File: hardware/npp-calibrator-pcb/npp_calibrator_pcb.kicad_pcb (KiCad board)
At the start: 2 copper layers, 80 x 34 mm, 7 parts, among them X1 SOIC16 Test Socket, X2 DE9_Plug, X3 DE9_Plug

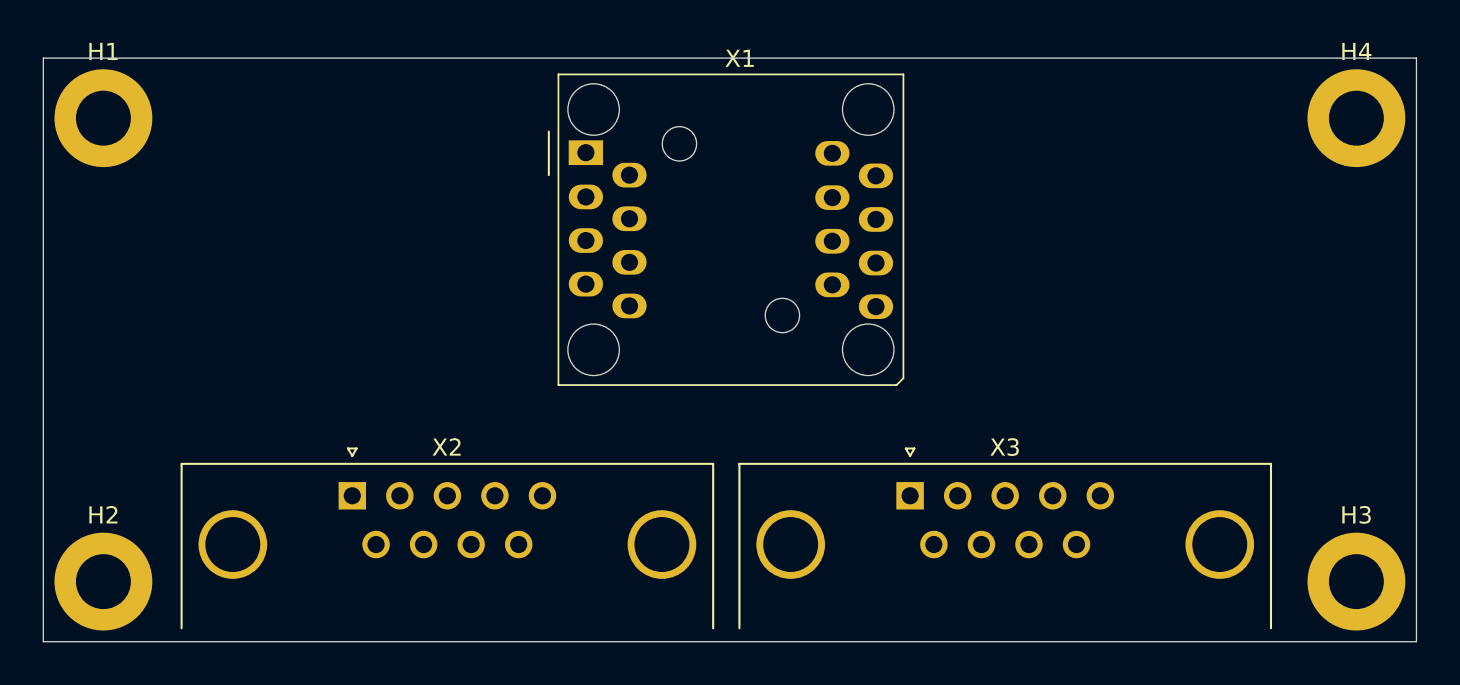
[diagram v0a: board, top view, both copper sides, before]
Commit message: Updates to calibration hardware
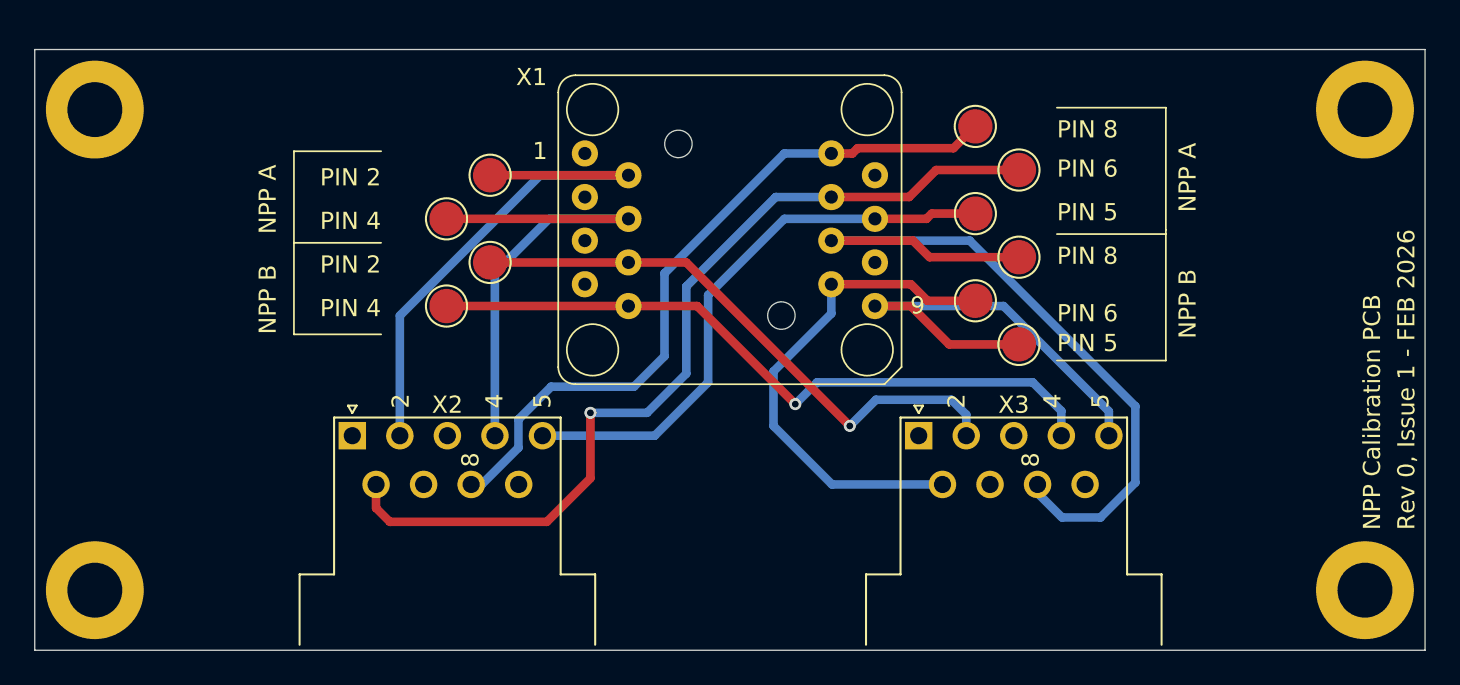
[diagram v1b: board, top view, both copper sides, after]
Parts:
- added TP1: TestPoint, TestPoint:TestPoint_Pad_D2.0mm, F.Cu at (114.3, 99.1)
- added TP10: TestPoint, TestPoint:TestPoint_Pad_D2.0mm, F.Cu at (114.3, 104.1)
- added TP2: TestPoint, TestPoint:TestPoint_Pad_D2.0mm, F.Cu at (83.5, 99.4)
- added TP3: TestPoint, TestPoint:TestPoint_Pad_D2.0mm, F.Cu at (114.3, 94.0)
- added TP4: TestPoint, TestPoint:TestPoint_Pad_D2.0mm, F.Cu at (86.0, 96.8)
- added TP5: TestPoint, TestPoint:TestPoint_Pad_D2.0mm, F.Cu at (116.8, 96.5)
- added TP6: TestPoint, TestPoint:TestPoint_Pad_D2.0mm, F.Cu at (116.8, 106.7)
- added TP7: TestPoint, TestPoint:TestPoint_Pad_D2.0mm, F.Cu at (83.5, 104.4)
- added TP8: TestPoint, TestPoint:TestPoint_Pad_D2.0mm, F.Cu at (116.8, 101.6)
- added TP9: TestPoint, TestPoint:TestPoint_Pad_D2.0mm, F.Cu at (86.0, 101.9)
- X1: footprint Socket:SOIC_Socket_16_SOCKET-SOICN-16-1.27 -> NPP_Calbrator:PA-SOCKET-SOICN-16-1.27
- X2, X3: footprint Connector_Dsub:DSUB-9_Male_Horizontal_P2.77x2.84mm_EdgePinOffset4.94mm_Housed_MountingHolesOffset4.94mm -> Connector_Dsub:DSUB-9_Male_Horizontal_P2.77x2.84mm_EdgePinOffset9.40mm
- moved X1 9.50 mm to (100.0, 100.0)
- moved X3 3.54 mm to (111.0, 112.0)
- moved X2 3.50 mm to (78.0, 112.0)
- moved H1 0.71 mm to (137.0, 93.0)
- moved H2 0.71 mm to (137.0, 121.0)
- moved H3 0.71 mm to (63.0, 121.0)
- moved H4 0.71 mm to (63.0, 93.0)
- renumbered H4 to H1, H3 to H2, H2 to H3, H1 to H4
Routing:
- net /A6: track 0.00 -> 52.9 mm, vias 0 -> 1
- net /B8: track 0.00 -> 45.3 mm
- net /A8: track 0.00 -> 41.8 mm
- net /B4: track 0.00 -> 40.8 mm, vias 0 -> 1
- net /B2: track 0.00 -> 33.9 mm, vias 0 -> 1
- net /A5: track 0.00 -> 33.6 mm
- net /A2: track 0.00 -> 31.8 mm
- net /B6: track 0.00 -> 29.2 mm
- net /A4: track 0.00 -> 29.2 mm
- net /B5: track 0.00 -> 26.9 mm
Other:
- board size 80 x 34 mm -> 81 x 35 mm
- board text added: "2"
- board text added: "4"
- board text added: "5"
- board text added: "8"
- board text added: "NPP A"
- board text added: "NPP B"
- board text added: "NPP Calibration PCB"
- board text added: "PIN 2"
- board text added: "PIN 4"
- board text added: "PIN 5"
- board text added: "PIN 6"
- board text added: "PIN 8"
- board text added: "Rev 0, Issue 1 - FEB 2026"
